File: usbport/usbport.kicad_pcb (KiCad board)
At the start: 2 copper layers, 60 x 17 mm, 4 parts, among them J1 USB1110-XX-X_REVA, J2 USB1110-XX-X_REVA, J3 Conn_01x10_Male, J4 Conn_01x10_Male

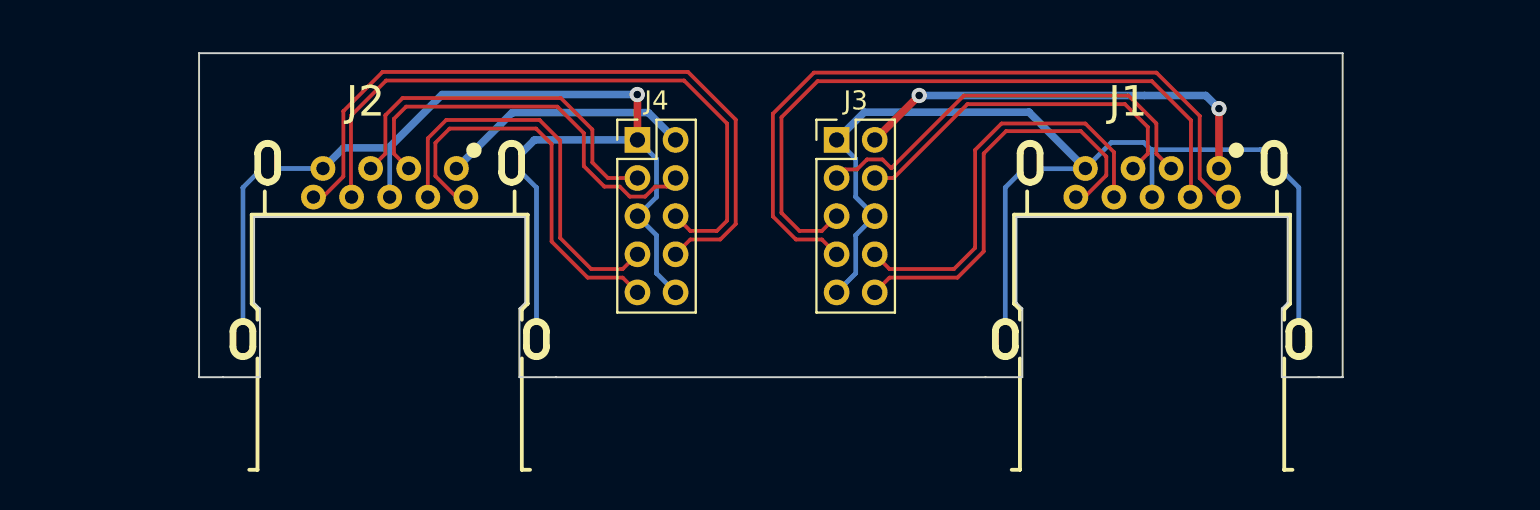
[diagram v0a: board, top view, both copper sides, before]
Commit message: update goose45 pcb board edge comment
* goose45 - update board layout
* usbport - change edge size and add edge comment
* usbhub2.0 - change layout and the footprint
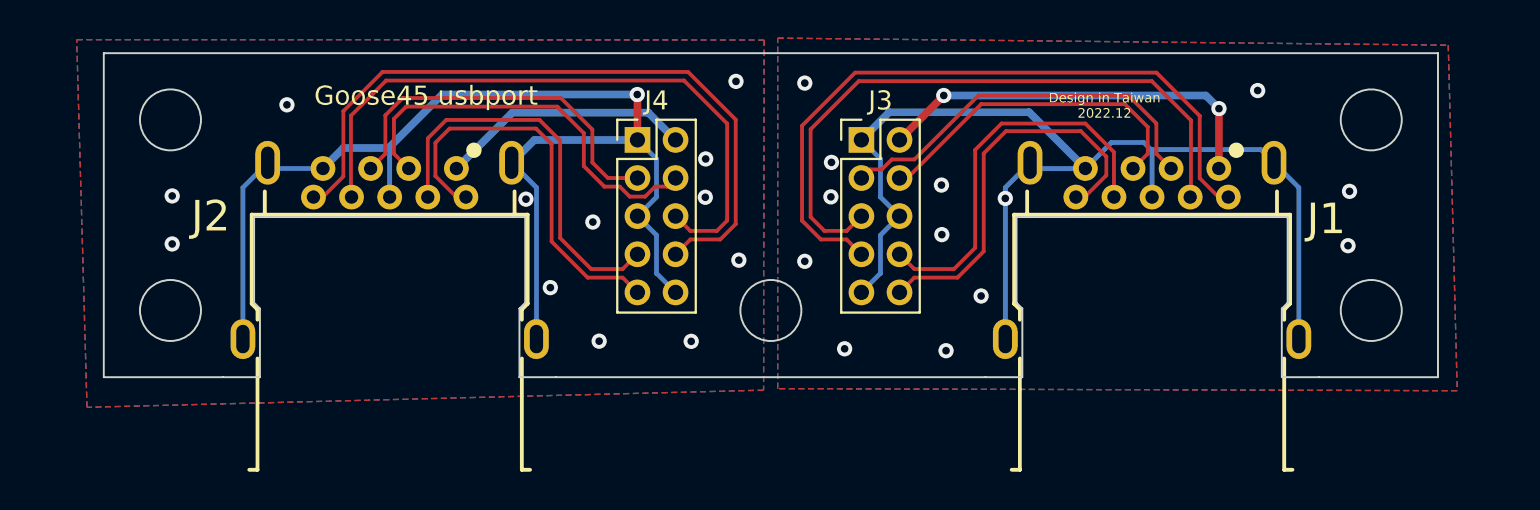
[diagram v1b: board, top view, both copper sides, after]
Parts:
- moved J3 1.30 mm to (134.8, 34.5)
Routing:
- net J1_STDA_SSTX-: track 35.8 -> 33.8 mm
- net J1_STDA_SSTX+: track 39.0 -> 37.0 mm
- net J1_D-: track 22.2 -> 20.6 mm
- net J1_STDA_SSRX-: track 22.3 -> 21.0 mm
- net J1_STDA_SSRX+: track 22.0 -> 20.7 mm
- net J1_D+: track 18.9 -> 17.6 mm
- net J1_GND: track 60.6 -> 59.3 mm, vias 0 -> 13
- net J1_VBUS: track 22.5 -> 21.2 mm
- net J2_GND: vias 1 -> 13
- added copper zone on B.Cu, net J1_GND
- added copper zone on F.Cu, net J1_GND
- added copper zone on B.Cu, net J2_GND
- added copper zone on F.Cu, net J2_GND
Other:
- board size 60 x 17 mm -> 70 x 17 mm
- board text added: "Design in Taiwan 2022.12"
- board text added: "Goose45 usbport"

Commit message: update pcb common and update goose45 key loaction
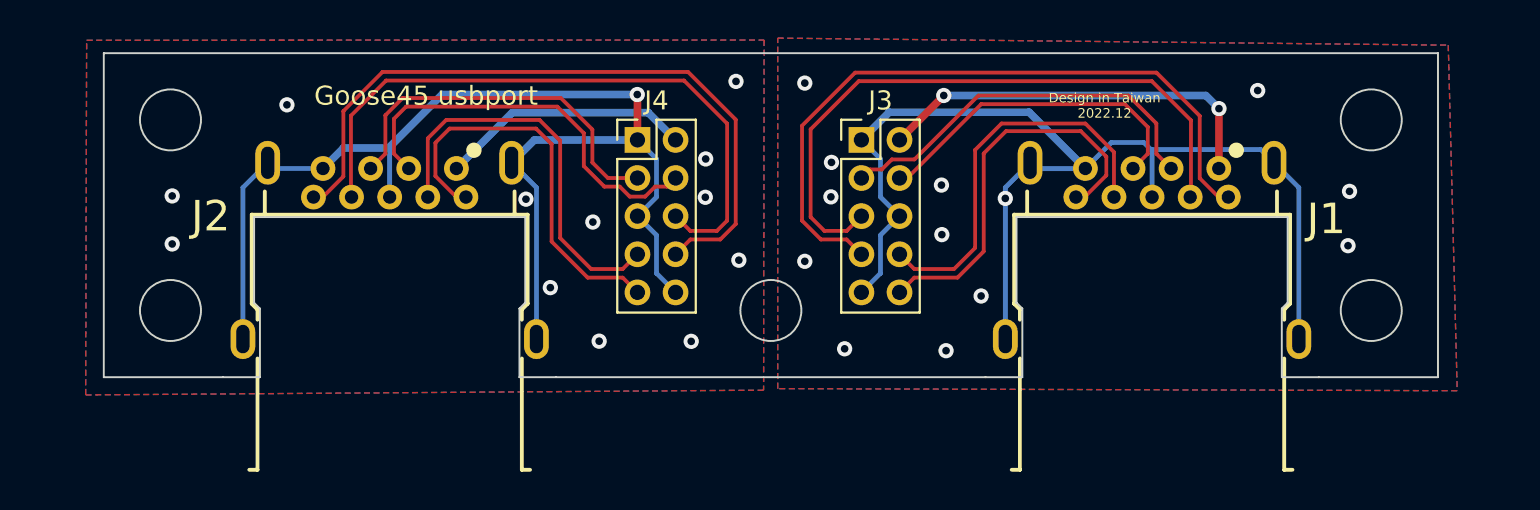
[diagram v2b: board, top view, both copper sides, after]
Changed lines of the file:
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@@
+  )
+  (dimension (type aligned) (layer "Cmts.User")
+    (pts (xy 110 45) (xy 150 45))
+    (height -18.29)
+    (gr_text "40.0000 mm" (at 130 25.56) (layer "Cmts.User")
+      (effects (font (size 1 1) (thickness 0.15)))
+    )
+    (format (units 3) (units_format 1) (precision 4))
+    (style (thickness 0.15) (arrow_length 1.27) (text_position_mode 0) (extension_height 0.58642) (extension_offset 0.5) keep_text_aligned)
   )
   (dimension (type aligned) (layer "Cmts.User")
@@
     (gr_text "3.5000 mm" (at 184.41 45.25 90) (layer "Cmts.User")
       (effects (font (size 1 1) (thickness 0.15)) (justify left))
+    )
+    (format (units 3) (units_format 1) (precision 4))
+    (style (thickness 0.15) (arrow_length 1.27) (text_position_mode 0) (extension_height 0.58642) (extension_offset 0.5) keep_text_aligned)
+  )
+  (dimension (type aligned) (layer "Cmts.User")
+    (pts (xy 150 43.5) (xy 161.5 43.5))
+    (height 10.97)
+    (gr_text "11.5000 mm" (at 155.75 53.32) (layer "Cmts.User")
+      (effects (font (size 1 1) (thickness 0.15)))
     )
     (format (units 3) (units_format 1) (precision 4))
@@
         (xy 129.647637 29.310045)
         (xy 129.617637 47.680045)
-        (xy 94.119309 48.579607)
-        (xy 93.579309 29.289607)
+        (xy 94.05 47.93)
+        (xy 94.1 29.32)
       )
     )

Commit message: update usbport pcb edge size comments
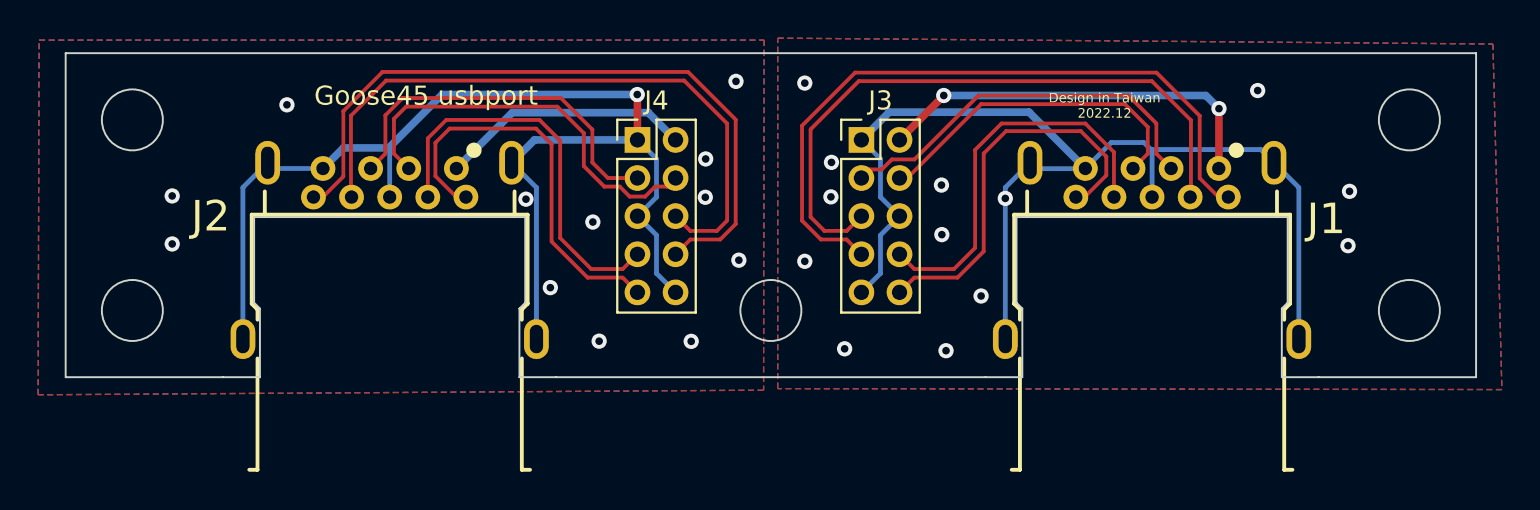
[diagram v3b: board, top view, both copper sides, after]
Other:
- board size 70 x 17 mm -> 74 x 17 mm
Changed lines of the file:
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@@
     )
   )
-  (gr_line (start 95 30) (end 165 30) (layer "Edge.Cuts") (width 0.1))
-  (gr_line (start 165 47) (end 165 30) (layer "Edge.Cuts") (width 0.1))
+  (gr_line (start 93 30) (end 167 30) (layer "Edge.Cuts") (width 0.1))
+  (gr_line (start 167 47) (end 167 30) (layer "Edge.Cuts") (width 0.1))
   (gr_circle (center 130 43.5) (end 131.6 43.5) (layer "Edge.Cuts") (width 0.1) (fill none))
-  (gr_line locked (start 158.7376 47) (end 165 47) (layer "Edge.Cuts") (width 0.1))
-  (gr_circle locked (center 98.5 43.5) (end 100.1 43.5) (layer "Edge.Cuts") (width 0.1) (fill none))
-  (gr_line locked (start 95 47) (end 101.2624 47) (layer "Edge.Cuts") (width 0.1))
-  (gr_circle locked (center 161.5 43.5) (end 163.1 43.5) (layer "Edge.Cuts") (width 0.1) (fill none))
-  (gr_circle locked (center 161.5 33.5) (end 163.1 33.5) (layer "Edge.Cuts") (width 0.1) (fill none))
-  (gr_line (start 95 47) (end 95 30) (layer "Edge.Cuts") (width 0.1))
-  (gr_circle locked (center 98.5 33.5) (end 100.1 33.5) (layer "Edge.Cuts") (width 0.1) (fill none))
+  (gr_line locked (start 158.7376 47) (end 167 47) (layer "Edge.Cuts") (width 0.1))
+  (gr_circle locked (center 96.5 43.5) (end 98.1 43.5) (layer "Edge.Cuts") (width 0.1) (fill none))
+  (gr_line locked (start 93 47) (end 101.2624 47) (layer "Edge.Cuts") (width 0.1))
+  (gr_circle locked (center 163.5 43.5) (end 165.1 43.5) (layer "Edge.Cuts") (width 0.1) (fill none))
+  (gr_circle locked (center 163.5 33.5) (end 165.1 33.5) (layer "Edge.Cuts") (width 0.1) (fill none))
+  (gr_line (start 93 47) (end 93 30) (layer "Edge.Cuts") (width 0.1))
+  (gr_circle locked (center 96.5 33.5) (end 98.1 33.5) (layer "Edge.Cuts") (width 0.1) (fill none))
   (gr_line locked (start 118.7376 47) (end 141.2624 47) (layer "Edge.Cuts") (width 0.1))
   (gr_text "Design in Taiwan\n2022.12" (at 147.51 32.75) (layer "F.SilkS")
@@
   )
   (dimension (type aligned) (layer "Cmts.User")
-    (pts (xy 95 30) (xy 165 30))
-    (height -7.51)
-    (gr_text "70.0000 mm" (at 130 21.34) (layer "Cmts.User")
-      (effects (font (size 1 1) (thickness 0.15)))
-    )
-    (format (units 3) (units_format 1) (precision 4))
-    (style (thickness 0.15) (arrow_length 1.27) (text_position_mode 0) (extension_height 0.58642) (extension_offset 0.5) keep_text_aligned)
-  )
-  (dimension (type aligned) (layer "Cmts.User")
-    (pts (xy 161.5 43.5) (xy 165 43.5))
-    (height 15.18)
-    (gr_text "3.5000 mm" (at 163.25 57.53) (layer "Cmts.User")
-      (effects (font (size 1 1) (thickness 0.15)) (justify left))
-    )
-    (format (units 3) (units_format 1) (precision 4))
-    (style (thickness 0.15) (arrow_length 1.27) (text_position_mode 0) (extension_height 0.58642) (extension_offset 0.5) keep_text_aligned)
-  )
-  (dimension (type aligned) (layer "Cmts.User")
     (pts (xy 110 45) (xy 150 45))
     (height -18.29)
@@
   )
   (dimension (type aligned) (layer "Cmts.User")
-    (pts (xy 161.5 41.9) (xy 161.5 45.1))
-    (height -18.5)
-    (gr_text "3.2000 mm" (at 178.85 43.5 90) (layer "Cmts.User")
-      (effects (font (size 1 1) (thickness 0.15)) (justify left))
-    )
-    (format (units 3) (units_format 1) (precision 4))
-    (style (thickness 0.15) (arrow_length 1.27) (text_position_mode 0) (extension_height 0.58642) (extension_offset 0.5) keep_text_aligned)
-  )
-  (dimension (type aligned) (layer "Cmts.User")
-    (pts (xy 130 43.5) (xy 161.5 43.5))
-    (height 15.25)
-    (gr_text "31.5000 mm" (at 145.75 57.6) (layer "Cmts.User")
-      (effects (font (size 1 1) (thickness 0.15)) (justify left))
+    (pts (xy 163.5 45.1) (xy 163.5 41.9))
+    (height 16.48)
+    (gr_text "3.2000 mm" (at 178.83 43.5 90) (layer "Cmts.User")
+      (effects (font (size 1 1) (thickness 0.15)) (justify left))
+    )
+    (format (units 3) (units_format 1) (precision 4))
+    (style (thickness 0.15) (arrow_length 1.27) (text_position_mode 0) (extension_height 0.58642) (extension_offset 0.5) keep_text_aligned)
+  )
+  (dimension (type aligned) (layer "Cmts.User")
+    (pts (xy 93 30) (xy 167 30))
+    (height -8.48)
+    (gr_text "74.0000 mm" (at 130 20.37) (layer "Cmts.User")
+      (effects (font (size 1 1) (thickness 0.15)))
     )
     (format (units 3) (units_format 1) (precision 4))
@@
   )
   (dimension (type aligned) (layer "Cmts.User")
+    (pts (xy 130 43.5) (xy 163.5 43.5))
+    (height 13.9)
+    (gr_text "33.5000 mm" (at 146.75 56.25) (layer "Cmts.User")
+      (effects (font (size 1 1) (thickness 0.15)))
+    )
+    (format (units 3) (units_format 1) (precision 4))
+    (style (thickness 0.15) (arrow_length 1.27) (text_position_mode 0) (extension_height 0.58642) (extension_offset 0.5) keep_text_aligned)
+  )
+  (dimension (type aligned) (layer "Cmts.User")
     (pts (xy 116.807 47) (xy 143.193 47))
     (height 20.77)
@@
   )
   (dimension (type aligned) (layer "Cmts.User")
-    (pts (xy 161.5 43.5) (xy 161.5 33.5))
-    (height 13.24)
-    (gr_text "10.0000 mm" (at 173.59 38.5 90) (layer "Cmts.User")
-      (effects (font (size 1 1) (thickness 0.15)) (justify left))
-    )
-    (format (units 3) (units_format 1) (precision 4))
-    (style (thickness 0.15) (arrow_length 1.27) (text_position_mode 0) (extension_height 0.58642) (extension_offset 0.5) keep_text_aligned)
-  )
-  (dimension (type aligned) (layer "Cmts.User")
-    (pts (xy 95 47) (xy 95 30))
-    (height -7.75)
-    (gr_text "17.0000 mm" (at 86.1 38.5 90) (layer "Cmts.User")
-      (effects (font (size 1 1) (thickness 0.15)))
-    )
-    (format (units 3) (units_format 1) (precision 4))
-    (style (thickness 0.15) (arrow_length 1.27) (text_position_mode 0) (extension_height 0.58642) (extension_offset 0.5) keep_text_aligned)
-  )
-  (dimension (type aligned) (layer "Cmts.User")
-    (pts (xy 161.5 43.5) (xy 161.5 47))
-    (height -24.06)
-    (gr_text "3.5000 mm" (at 184.41 45.25 90) (layer "Cmts.User")
-      (effects (font (size 1 1) (thickness 0.15)) (justify left))
-    )
-    (format (units 3) (units_format 1) (precision 4))
-    (style (thickness 0.15) (arrow_length 1.27) (text_position_mode 0) (extension_height 0.58642) (extension_offset 0.5) keep_text_aligned)
-  )
-  (dimension (type aligned) (layer "Cmts.User")
-    (pts (xy 150 43.5) (xy 161.5 43.5))
-    (height 10.97)
-    (gr_text "11.5000 mm" (at 155.75 53.32) (layer "Cmts.User")
-      (effects (font (size 1 1) (thickness 0.15)))
-    )
-    (format (units 3) (units_format 1) (precision 4))
-    (style (thickness 0.15) (arrow_length 1.27) (text_position_mode 0) (extension_height 0.58642) (extension_offset 0.5) keep_text_aligned)
-  )
-  (dimension (type aligned) (layer "Cmts.User")
-    (pts (xy 98.5 43.5) (xy 161.5 43.5))
-    (height 31.75)
-    (gr_text "63.0000 mm" (at 130 74.1) (layer "Cmts.User")
+    (pts (xy 96.5 43.5) (xy 163.5 43.5))
+    (height 29.44)
+    (gr_text "67.0000 mm" (at 130 71.79) (layer "Cmts.User")
+      (effects (font (size 1 1) (thickness 0.15)))
+    )
+    (format (units 3) (units_format 1) (precision 4))
+    (style (thickness 0.15) (arrow_length 1.27) (text_position_mode 0) (extension_height 0.58642) (extension_offset 0.5) keep_text_aligned)
+  )
+  (dimension (type aligned) (layer "Cmts.User")
+    (pts (xy 150 43.5) (xy 163.49 43.5))
+    (height 11.31)
+    (gr_text "13.4900 mm" (at 156.745 53.66) (layer "Cmts.User")
+      (effects (font (size 1 1) (thickness 0.15)))
+    )
+    (format (units 3) (units_format 1) (precision 4))
+    (style (thickness 0.15) (arrow_length 1.27) (text_position_mode 0) (extension_height 0.58642) (extension_offset 0.5) keep_text_aligned)
+  )
+  (dimension (type aligned) (layer "Cmts.User")
+    (pts (xy 93 30) (xy 93 47))
+    (height 6.53)
+    (gr_text "17.0000 mm" (at 85.32 38.5 90) (layer "Cmts.User")
+      (effects (font (size 1 1) (thickness 0.15)))
+    )
+    (format (units 3) (units_format 1) (precision 4))
+    (style (thickness 0.15) (arrow_length 1.27) (text_position_mode 0) (extension_height 0.58642) (extension_offset 0.5) keep_text_aligned)
+  )
+  (dimension (type aligned) (layer "Cmts.User")
+    (pts (xy 161.9 43.5) (xy 165.1 43.5))
+    (height 9.2)
+    (gr_text "3.2000 mm" (at 163.5 51.55) (layer "Cmts.User")
+      (effects (font (size 1 1) (thickness 0.15)) (justify left))
+    )
+    (format (units 3) (units_format 1) (precision 4))
+    (style (thickness 0.15) (arrow_length 1.27) (text_position_mode 0) (extension_height 0.58642) (extension_offset 0.5) keep_text_aligned)
+  )
+  (dimension (type aligned) (layer "Cmts.User")
+    (pts (xy 163.5 43.5) (xy 163.5 33.5))
+    (height 11.34)
+    (gr_text "10.0000 mm" (at 173.69 38.5 90) (layer "Cmts.User")
+      (effects (font (size 1 1) (thickness 0.15)) (justify left))
+    )
+    (format (units 3) (units_format 1) (precision 4))
+    (style (thickness 0.15) (arrow_length 1.27) (text_position_mode 0) (extension_height 0.58642) (extension_offset 0.5) keep_text_aligned)
+  )
+  (dimension (type aligned) (layer "Cmts.User")
+    (pts (xy 163.5 47) (xy 163.5 43.5))
+    (height 21.25)
+    (gr_text "3.5000 mm" (at 183.6 45.25 90) (layer "Cmts.User")
       (effects (font (size 1 1) (thickness 0.15)) (justify left))
     )
@@
         (xy 129.647637 29.310045)
         (xy 129.617637 47.680045)
-        (xy 94.05 47.93)
-        (xy 94.1 29.32)
+        (xy 91.555251 47.923297)
+        (xy 91.605251 29.313297)
       )
     )
@@
     (polygon
       (pts
-        (xy 165.54 29.58)
-        (xy 166.01 47.71)
+        (xy 167.883042 29.519259)
+        (xy 168.353042 47.649259)
         (xy 130.36 47.6)
         (xy 130.36 29.21)
